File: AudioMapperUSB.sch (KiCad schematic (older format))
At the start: 152 parts, among them J1 USB_B, J10 Conn_01x01, J11 Conn_01x01, J12 Jack-DC, J16 Audio-Jack-2, J17 Audio-Jack-2, J18 Audio-Jack-2, J19 Audio-Jack-2, J2 Audio-Jack-2, J20 Audio-Jack-2, J21 Audio-Jack-2, J3 Conn_01x02, J4 Audio-Jack-2, J5 Conn_01x02, J6 Conn_01x02, J7 Conn_01x02, J8 Conn_01x01, J9 Conn_01x01, Q1 SS8550, U1 AMS1117-3.3, U2 PCM2900, U3 OPA2170, U4 OPA2170, U5 OPA2170, U6 OPA2170, U7 KA78M05_TO252, U8 74HC04, Y1 12 MHz

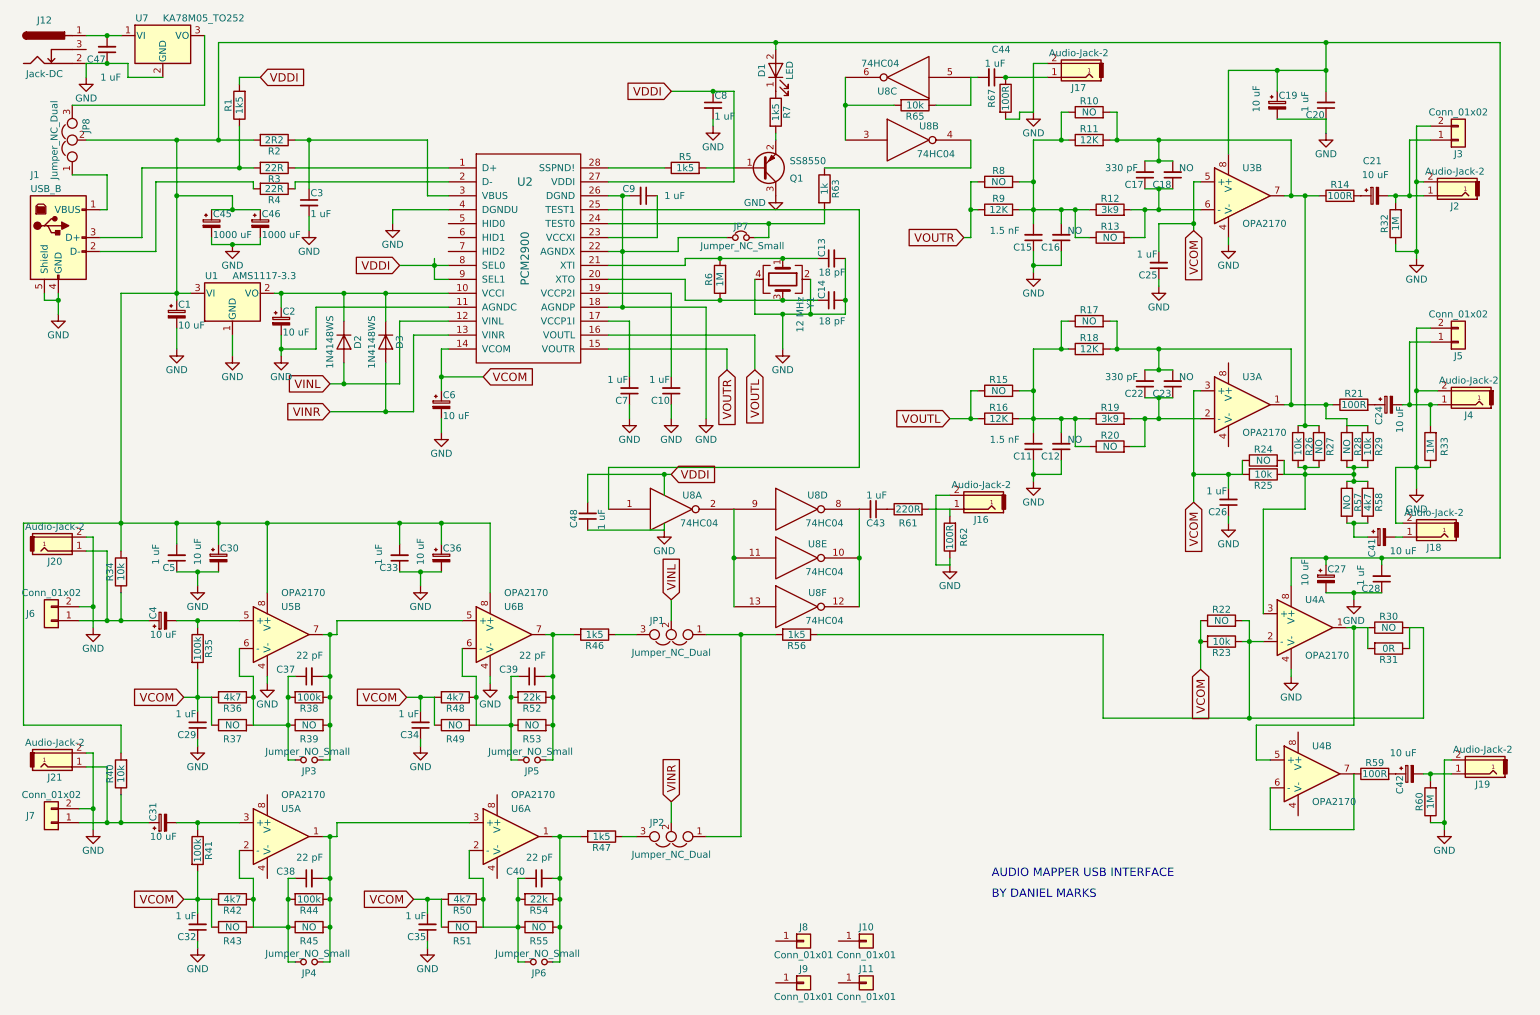
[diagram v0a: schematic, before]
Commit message: Fixed problem with VCOM leaking into input audio
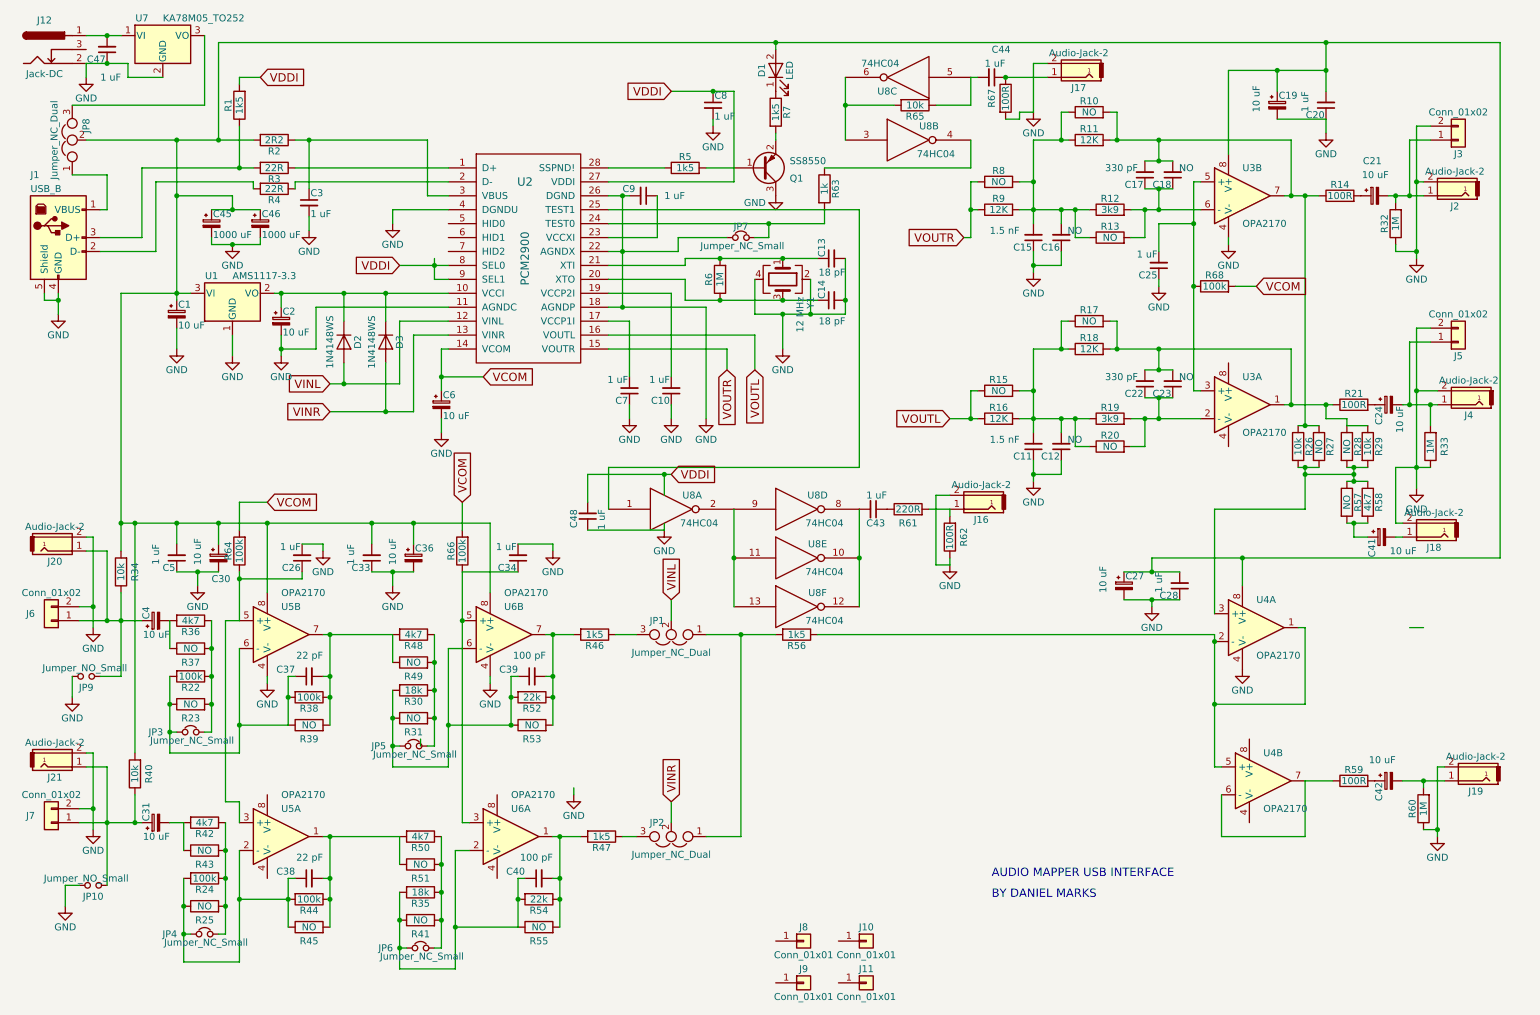
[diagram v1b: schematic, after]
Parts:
- removed C29, C32, C35: 1 uF, Capacitors_SMD:C_0805_HandSoldering, symbol C_Small
- removed JP3, JP4, JP5, JP6: Jumper_NO_Small, Pin_Headers:Pin_Header_Straight_1x02_Pitch2.54mm, symbol Jumper_NO_Small
- added JP10, JP9: Jumper_NO_Small, Pin_Headers:Pin_Header_Straight_1x02_Pitch2.54mm, symbol Jumper_NO_Small
- added JP3, JP4, JP5, JP6: Jumper_NC_Small, Pin_Headers:Pin_Header_Straight_1x02_Pitch2.54mm, symbol Jumper_NC_Small
- added R64, R66, R68: 100k, Resistors_SMD:R_0805_HandSoldering, symbol R
- C39, C40: value 22 pF -> 100 pF; LCSC C1804 -> C1790
- R22, R24: value NO -> 100k; footprint Resistors_THT:R_Axial_DIN0207_L6.3mm_D2.5mm_P7.62mm_Horizontal -> Resistors_SMD:R_0805_HandSoldering; LCSC (none) -> C17407
- R23, R25: value 10k -> NO; footprint Resistors_SMD:R_0805_HandSoldering -> Resistors_THT:R_Axial_DIN0207_L6.3mm_D2.5mm_P7.62mm_Horizontal; LCSC C17414 -> (none)
- R30: value NO -> 18k; footprint Resistors_THT:R_Axial_DIN0207_L6.3mm_D2.5mm_P7.62mm_Horizontal -> Resistors_SMD:R_0805_HandSoldering; LCSC (none) -> C17506
- R31: value 0R -> NO; footprint Resistors_SMD:R_0805_HandSoldering -> Resistors_THT:R_Axial_DIN0207_L6.3mm_D2.5mm_P7.62mm_Horizontal; LCSC C17477 -> (none)
- R35: value 100k -> 18k; LCSC C17407 -> C17506
- R41: value 100k -> NO; footprint Resistors_SMD:R_0805_HandSoldering -> Resistors_THT:R_Axial_DIN0207_L6.3mm_D2.5mm_P7.62mm_Horizontal; LCSC C17407 -> (none)
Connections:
- net GND: now also C26.2, C34.2, JP10.2, JP9.2; no longer C26.1, C34.1
- net VCOM: now also R64.2, R66.2, R68.2; no longer C25.2, C26.2, C34.2, R22.1, R23.2, R24.1, R25.2, R35.2, R36.2, R37.1, R41.2, R42.2, R43.1, R48.2, R49.1, R50.2, R51.1, U3.3 (+), U3.5 (+)
- net at C4.1, J20.1, J6.1 (Pin_1)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: now also JP9.1
- net at U4.1, U4.5 (+): now also R56.1, U4.2 (-); no longer R30.1, R31.2
- net at R26.2, R27.2, R28.2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: no longer R24.2, R25.1
- net at C37.1, R38.2, R39.1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: now also R22.2, R23.1, JP3.1; no longer R36.1, R37.2
- net at C37.2, R38.1, R39.2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: now also R48.2, R49.1; no longer U6.5 (+)
- net at C31.1, J21.1, J7.1 (Pin_1)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: now also JP10.1
- net at C38.2, R44.1, R45.2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: now also R50.2, R51.1; no longer U6.3 (+)
- net at C38.1, R44.2, R45.1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: now also R24.2, R25.1, JP4.1; no longer R42.1, R43.2
- net at C40.1, R54.2, R55.1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: now also R35.2, R41.1, JP6.1; no longer R50.1, R51.2
- net at C39.1, R52.2, R53.1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: now also R30.2, R31.1, JP5.1; no longer R48.1, R49.2
- new net: C4.2, R36.2, R37.1
- new net: C25.2, R68.1, U3.3 (+), U3.5 (+)
- new net: C26.1, R64.1, U5.3 (+), U5.5 (+)
- new net: JP3.2, R22.1, R23.2, R36.1, R37.2
- new net: C31.2, R42.2, R43.1
- new net: JP4.2, R24.1, R25.2, R42.1, R43.2
- new net: C34.1, R66.1, U6.3 (+), U6.5 (+)
- new net: JP5.2, R30.1, R31.2, R48.1, R49.2
- new net: JP6.2, R35.1, R41.2, R50.1, R51.2
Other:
- moved on the sheet: C27, C28, C31, C33, C34, C36, C4, C42, J19, R36, R37, R40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

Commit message: Added isolation between phantom power in mic channels
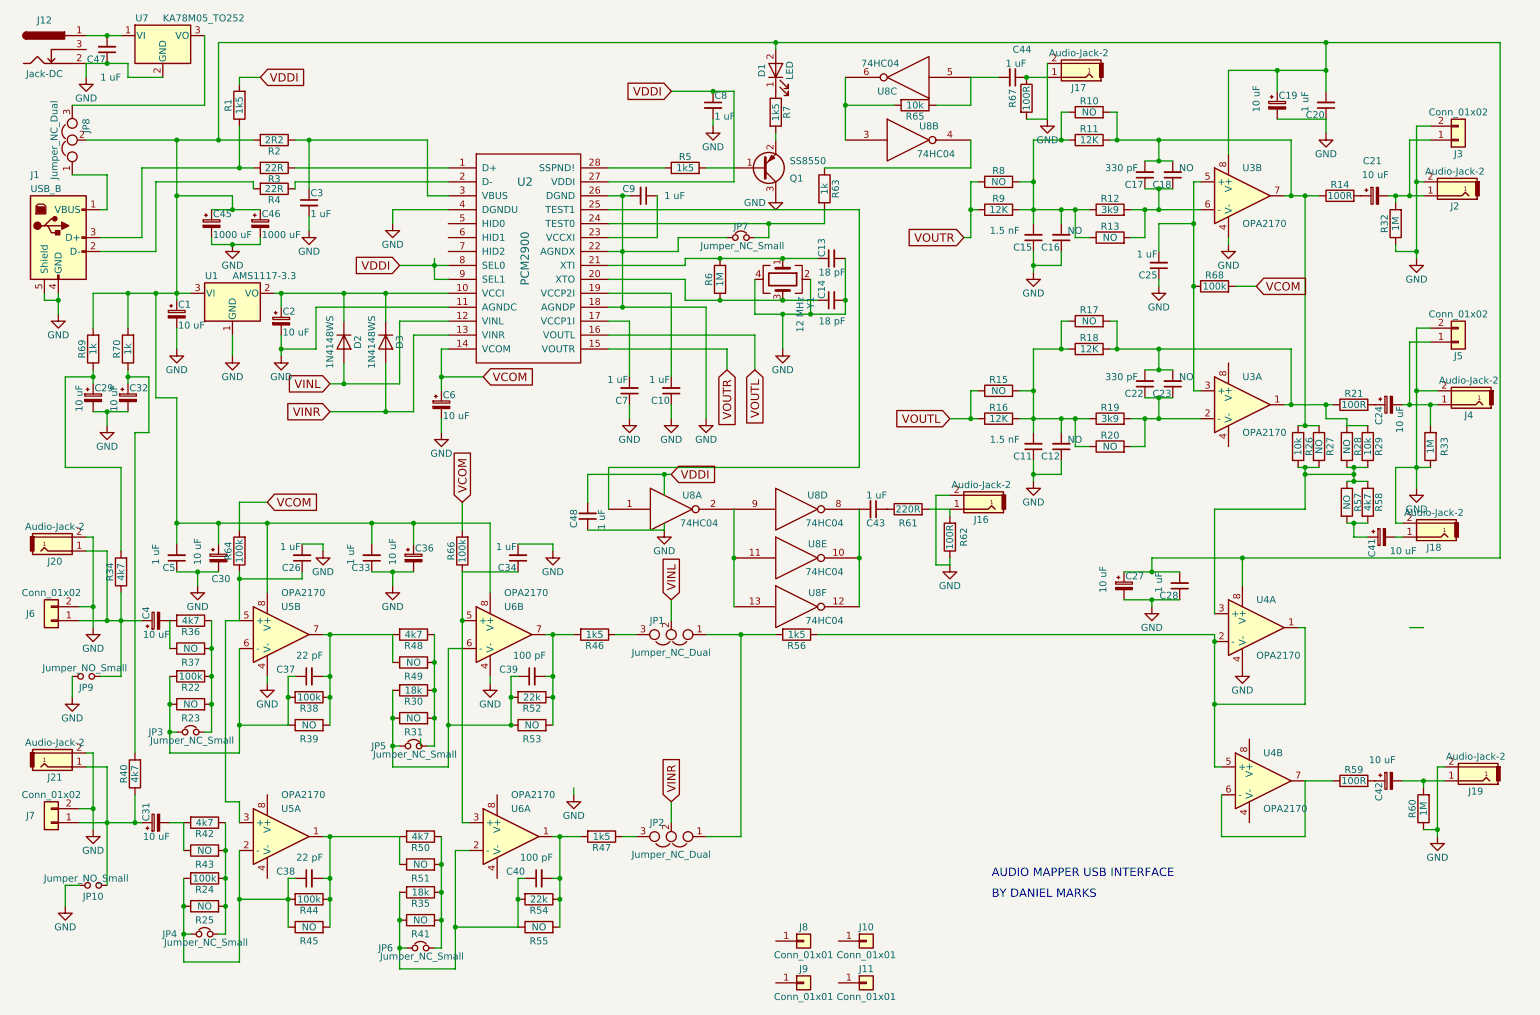
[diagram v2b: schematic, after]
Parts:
- added C29, C32: 10 uF, AudioMapperUSB:CP_1206_HandSoldering, symbol CP_Small
- added R69, R70: 1k, Resistors_SMD:R_0805_HandSoldering, symbol R
- R34, R40: value 10k -> 4k7; LCSC C17414 -> C17673
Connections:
- net GND: now also C29.2, C32.2
- net at C1.1, C19.1, C20.2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: now also R69.2, R70.2; no longer R34.2, R40.2
- new net: C29.1, R34.2, R69.1
- new net: C32.1, R40.2, R70.1
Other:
- moved on the sheet: C44, R67

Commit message: JLCPCB order 2021-01-31
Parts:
- added J13, J14: Conn_01x02, Connectors_Terminal_Blocks:TerminalBlock_bornier-2_P5.08mm, symbol Conn_01x02
- R34, R40: value 4k7 -> 10k; LCSC C17673 -> C17414
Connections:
- net GND: now also J13.2 (Pin_2), J14.2 (Pin_2)
- net at C41.2, J18.1: now also J13.1 (Pin_1)
- net at C42.2, J19.1, R60.2: now also J14.1 (Pin_1)
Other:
- moved on the sheet: C41
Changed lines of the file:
@@
 $EndComp
 $Comp
-L GND #PWR38
+L GND #PWR40
 U 1 1 5FEA8AA4
 P 10500 2250
-F 0 "#PWR38" H 10500 2000 50  0001 C CNN
+F 0 "#PWR40" H 10500 2000 50  0001 C CNN
 F 1 "GND" H 10500 2100 50  0000 C CNN
 F 2 "" H 10500 2250 50  0001 C CNN
@@
 $EndComp
 $Comp
-L GND #PWR39
+L GND #PWR41
 U 1 1 5FEA29F4
 P 10500 3900
-F 0 "#PWR39" H 10500 3650 50  0001 C CNN
+F 0 "#PWR41" H 10500 3650 50  0001 C CNN
 F 1 "GND" H 10500 3750 50  0000 C CNN
 F 2 "" H 10500 3900 50  0001 C CNN
@@
 $EndComp
 $Comp
-L GND #PWR40
+L GND #PWR42
 U 1 1 5FEF7E44
 P 10650 6400
-F 0 "#PWR40" H 10650 6150 50  0001 C CNN
+F 0 "#PWR42" H 10650 6150 50  0001 C CNN
 F 1 "GND" H 10650 6250 50  0000 C CNN
 F 2 "" H 10650 6400 50  0001 C CNN
@@
 L CP_Small C41
 U 1 1 5FEF86D3
-P 10250 4250
-F 0 "C41" H 10260 4320 50  0000 L CNN
-F 1 "10 uF" V 10350 4000 50  0000 L CNN
-F 2 "AudioMapperUSB:CP_1206_HandSoldering" H 10250 4250 50  0001 C CNN
-F 3 "" H 10250 4250 50  0001 C CNN
-F 4 " C7171" H 10250 4250 60  0001 C CNN "LCSC"
-	1    10250 4250
+P 10150 4250
+F 0 "C41" H 10160 4320 50  0000 L CNN
+F 1 "10 uF" V 10250 4000 50  0000 L CNN
+F 2 "AudioMapperUSB:CP_1206_HandSoldering" H 10150 4250 50  0001 C CNN
+F 3 "" H 10150 4250 50  0001 C CNN
+F 4 " C7171" H 10150 4250 60  0001 C CNN "LCSC"
+	1    10150 4250
 	0    -1   1    0
 $EndComp
@@
 $EndComp
 $Comp
-L GND #PWR21
-U 1 1 600BC99E
-P 4450 6100
-F 0 "#PWR21" H 4450 5850 50  0001 C CNN
-F 1 "GND" H 4450 5950 50  0000 C CNN
-F 2 "" H 4450 6100 50  0001 C CNN
-F 3 "" H 4450 6100 50  0001 C CNN
-	1    4450 6100
-	1    0    0    -1
-$EndComp
-$Comp
 L R R64
 U 1 1 600BFCA3
@@
 P 1200 4500
 F 0 "R34" V 1280 4500 50  0000 C CNN
-F 1 "4k7" V 1200 4500 50  0000 C CNN
+F 1 "10k" V 1200 4500 50  0000 C CNN
 F 2 "Resistors_SMD:R_0805_HandSoldering" V 1130 4500 50  0001 C CNN
 F 3 "" H 1200 4500 50  0001 C CNN
-F 4 "C17673" V 1200 4500 60  0001 C CNN "LCSC"
+F 4 "C17414" V 1200 4500 60  0001 C CNN "LCSC"
 	1    1200 4500
 	-1   0    0    1
@@
 P 1300 5950
 F 0 "R40" V 1380 5950 50  0000 C CNN
-F 1 "4k7" V 1300 5950 50  0000 C CNN
+F 1 "10k" V 1300 5950 50  0000 C CNN
 F 2 "Resistors_SMD:R_0805_HandSoldering" V 1230 5950 50  0001 C CNN
 F 3 "" H 1300 5950 50  0001 C CNN
-F 4 "C17673" V 1300 5950 60  0001 C CNN "LCSC"
+F 4 "C17414" V 1300 5950 60  0001 C CNN "LCSC"
 	1    1300 5950
 	-1   0    0    1
@@
 	10550 6350 10650 6350
 Wire Wire Line
-	10150 4250 10050 4250
-Wire Wire Line
-	10400 4250 10350 4250
+	10050 4250 10050 4250
+Wire Wire Line
+	10400 4250 10250 4250
 Wire Wire Line
 	10650 5900 10700 5900
@@
 Connection ~ 8600 4700
 Wire Wire Line
-	9600 5200 9600 5200
-Wire Wire Line
 	8600 4400 11100 4400
 Wire Wire Line
@@
 	9700 3800 10050 3800
 Connection ~ 10050 3750
-Wire Wire Line
-	10550 4900 10450 4900
 Wire Wire Line
 	11100 4400 11100 700
@@
 	800  6750 900  6750
 Wire Wire Line
-	10550 6000 10550 6050
+	10550 5450 10550 6050
 Wire Wire Line
 	2050 6150 2050 6300
@@
 Connection ~ 1650 6900
 Wire Wire Line
-	2050 7300 1650 7300
-Wire Wire Line
-	2050 6500 2050 7300
+	1650 7300 2050 7300
+Wire Wire Line
+	2050 7300 2050 6500
 Connection ~ 1650 7100
 Wire Wire Line
@@
 Connection ~ 3600 7050
 Wire Wire Line
-	4450 6100 4450 6050
-Wire Wire Line
 	2050 4500 2050 4850
 Wire Wire Line
@@
 Wire Wire Line
 	7500 950  7300 950
+$Comp
+L Conn_01x02 J13
+U 1 1 601760B1
+P 10700 4750
+F 0 "J13" H 10700 4850 50  0000 C CNN
+F 1 "Conn_01x02" H 10700 4550 50  0000 C CNN
+F 2 "Connectors_Terminal_Blocks:TerminalBlock_bornier-2_P5.08mm" H 10700 4750 50  0001 C CNN
+F 3 "" H 10700 4750 50  0001 C CNN
+	1    10700 4750
+	1    0    0    1
+$EndComp
+$Comp
+L GND #PWR39
+U 1 1 6017676B
+P 10350 4850
+F 0 "#PWR39" H 10350 4600 50  0001 C CNN
+F 1 "GND" H 10350 4700 50  0000 C CNN
+F 2 "" H 10350 4850 50  0001 C CNN
+F 3 "" H 10350 4850 50  0001 C CNN
+	1    10350 4850
+	1    0    0    -1
+$EndComp
+Wire Wire Line
+	10350 4850 10350 4650
+Wire Wire Line
+	10350 4650 10500 4650
+Wire Wire Line
+	10500 4750 10400 4750
+Wire Wire Line
+	10400 4750 10400 4250
+$Comp
+L Conn_01x02 J14
+U 1 1 6017710A
+P 11050 5450
+F 0 "J14" H 11050 5550 50  0000 C CNN
+F 1 "Conn_01x02" H 11050 5250 50  0000 C CNN
+F 2 "Connectors_Terminal_Blocks:TerminalBlock_bornier-2_P5.08mm" H 11050 5450 50  0001 C CNN
+F 3 "" H 11050 5450 50  0001 C CNN
+	1    11050 5450
+	1    0    0    1
+$EndComp
+$Comp
+L GND #PWR38
+U 1 1 6017771D
+P 10250 5600
+F 0 "#PWR38" H 10250 5350 50  0001 C CNN
+F 1 "GND" H 10250 5450 50  0000 C CNN
+F 2 "" H 10250 5600 50  0001 C CNN
+F 3 "" H 10250 5600 50  0001 C CNN
+	1    10250 5600
+	1    0    0    -1
+$EndComp
+Wire Wire Line
+	10250 5600 10250 5350
+Wire Wire Line
+	10250 5350 10850 5350
+Wire Wire Line
+	10550 5450 10850 5450
 $EndSCHEMATC

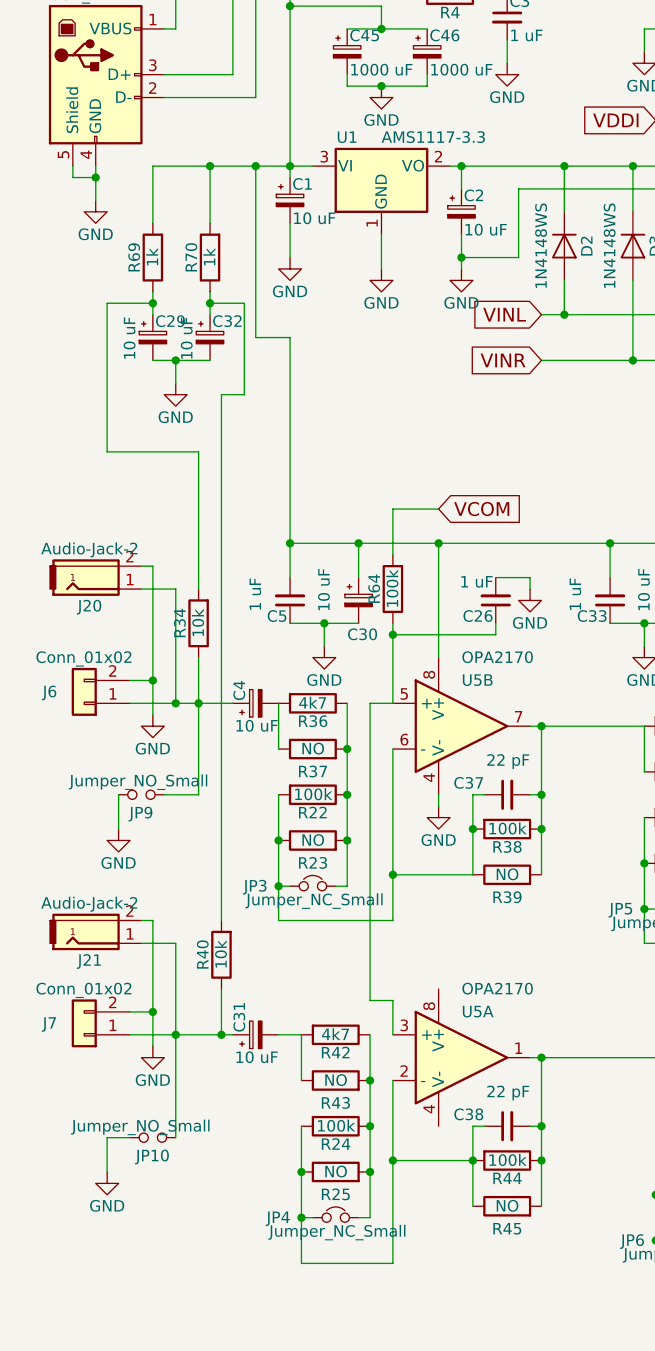
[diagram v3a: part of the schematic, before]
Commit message: Added source code of Audiomapper
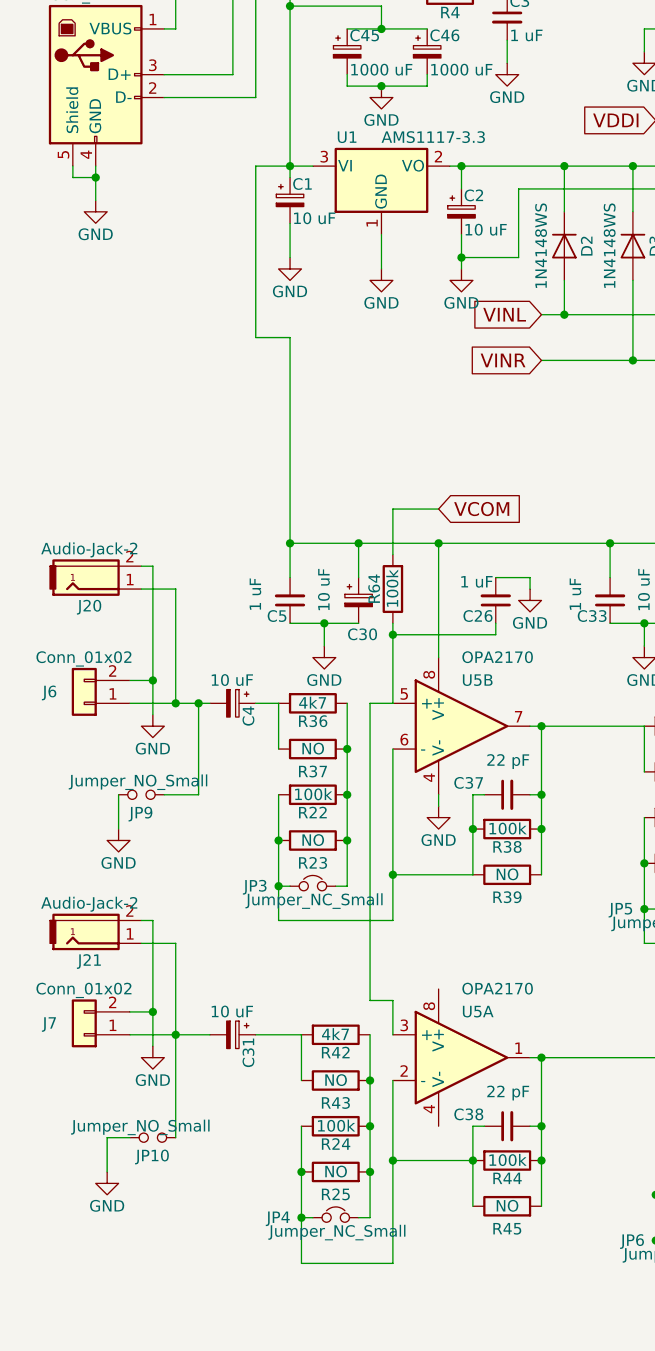
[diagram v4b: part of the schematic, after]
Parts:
- removed C29, C32: 10 uF, AudioMapperUSB:CP_1206_HandSoldering, symbol CP_Small
- removed R34, R40: 10k, Resistors_SMD:R_0805_HandSoldering, symbol R
- removed R69, R70: 1k, Resistors_SMD:R_0805_HandSoldering, symbol R
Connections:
- net at J20.1, J6.1 (Pin_1), JP9.1: now also C4.2; no longer C4.1
- net at R36.2, R37.1: now also C4.1; no longer C4.2
- net at J21.1, J7.1 (Pin_1), JP10.1: now also C31.2; no longer C31.1
- net at R42.2, R43.1: now also C31.1; no longer C31.2
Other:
- moved on the sheet: C31, C4
